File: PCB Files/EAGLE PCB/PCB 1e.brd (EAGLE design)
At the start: 45 x 75 mm, 31 parts

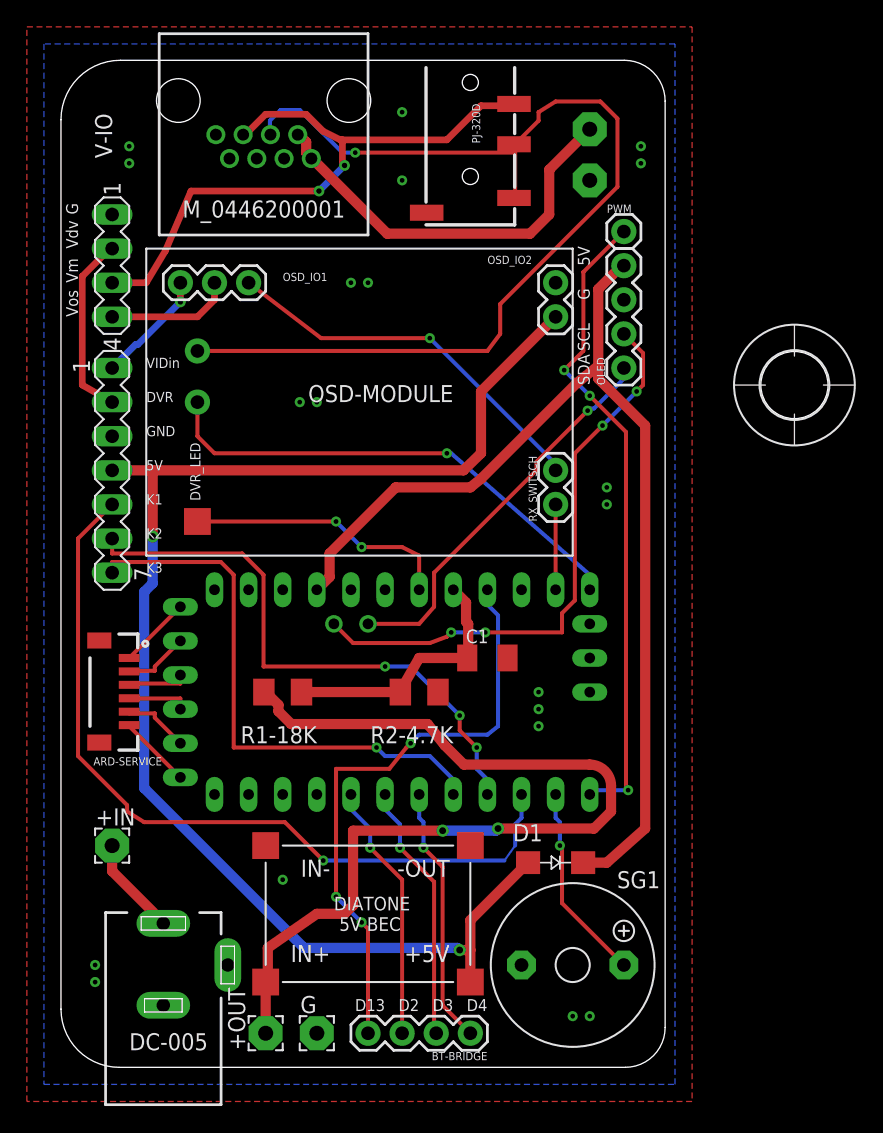
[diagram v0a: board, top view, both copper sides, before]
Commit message: new pcb1 revision 3 (5v on RJ45 and OSD PCB footprint added)
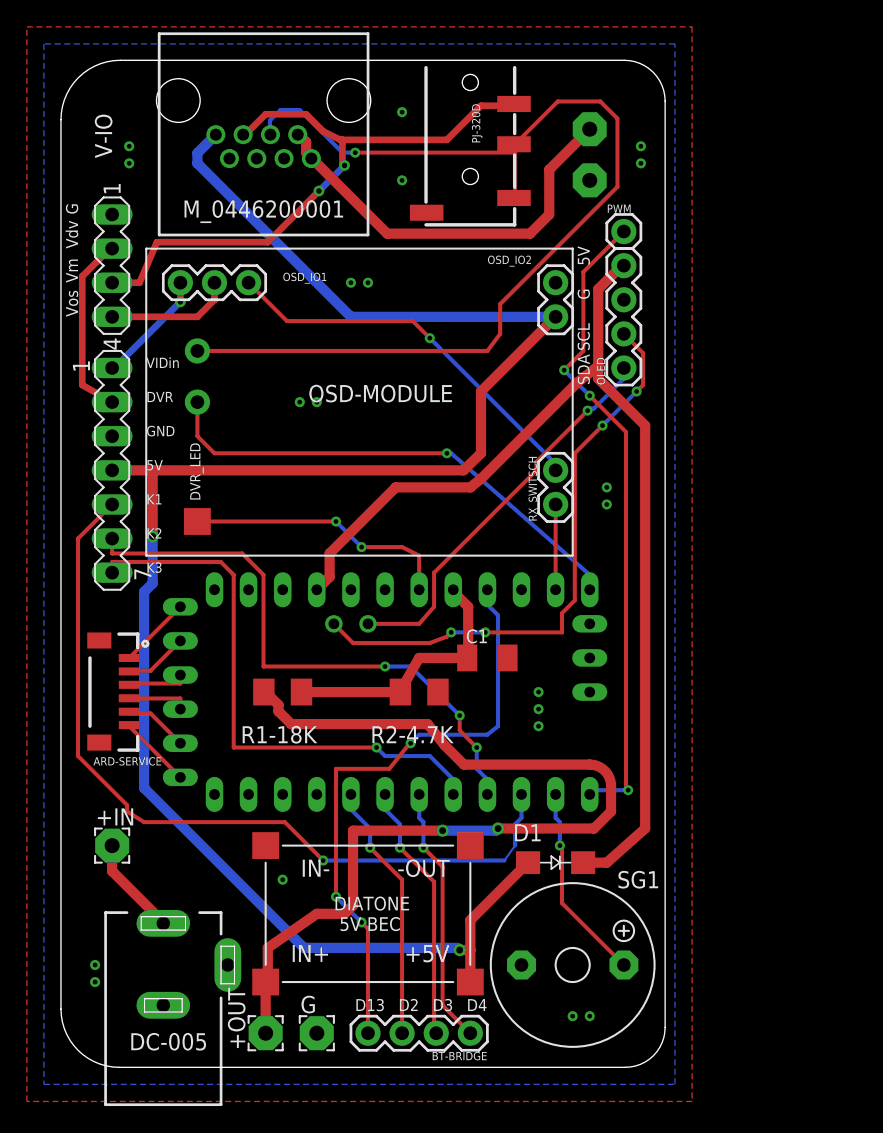
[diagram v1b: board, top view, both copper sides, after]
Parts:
- removed U$2: (no value), holes:5,0
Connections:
- net +5V: now also M_0446200001.1
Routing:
- net +5V: track 104.3 -> 138.4 mm
- net VMAIN: track 46.9 -> 46.2 mm

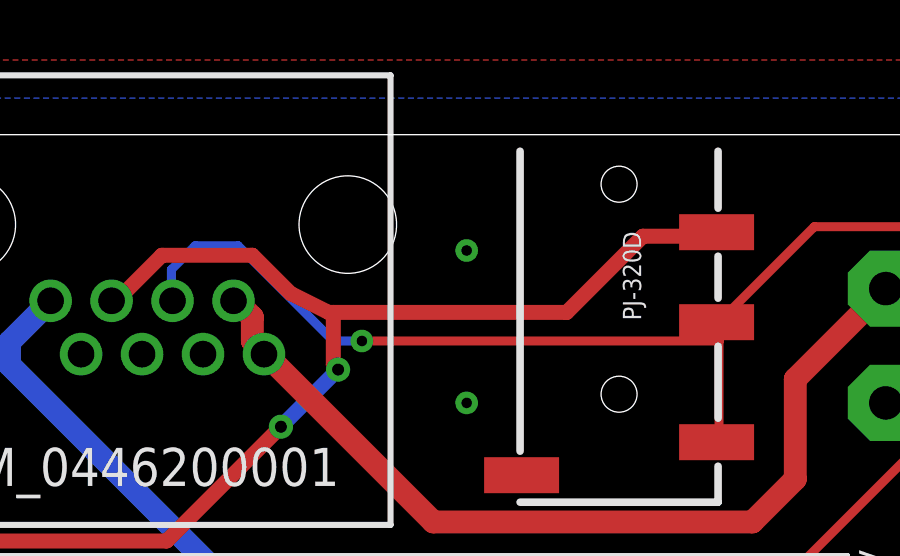
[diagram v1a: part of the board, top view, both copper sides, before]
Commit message: added 75ohm resistor to pcb
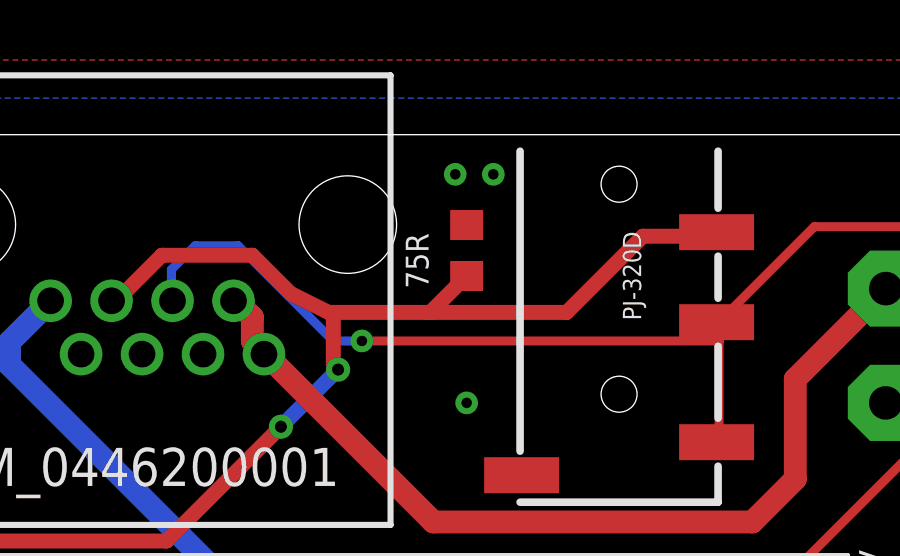
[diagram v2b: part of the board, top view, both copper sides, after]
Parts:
- added 75R: 75, resistor:R0603
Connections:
- net GND: now also 75R.2
- net VMAIN: now also 75R.1
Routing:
- net VMAIN: track 46.2 -> 47.9 mm
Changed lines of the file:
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@@
 <attribute name="VALUE" x="7.62" y="56.388" size="0.6096" layer="27" font="vector" ratio="20"/>
+</element>
+<element name="75R" library="resistor" library_urn="urn:adsk.eagle:library:348" package="R0603" package3d_urn="urn:adsk.eagle:package:23555/2" value="75" x="25.4" y="71.12" smashed="yes" rot="R90">
+<attribute name="NAME" x="24.13" y="69.85" size="0.762" layer="25" rot="R90"/>
+<attribute name="VALUE" x="27.94" y="69.85" size="1.27" layer="27" rot="R90"/>
 </element>
 </elements>
@@
 <via x="5.08" y="68.58" extent="1-16" drill="0.35"/>
 <via x="5.08" y="67.31" extent="1-16" drill="0.35"/>
-<via x="25.4" y="71.12" extent="1-16" drill="0.35"/>
+<via x="25.019" y="73.66" extent="1-16" drill="0.35"/>
 <via x="25.4" y="66.04" extent="1-16" drill="0.35"/>
 <via x="43.18" y="67.31" extent="1-16" drill="0.35"/>
@@
 <via x="40.64" y="43.18" extent="1-16" drill="0.35"/>
 <via x="40.64" y="41.91" extent="1-16" drill="0.35"/>
+<contactref element="75R" pad="2"/>
+<via x="26.289" y="73.66" extent="1-16" drill="0.35"/>
 </signal>
 <signal name="RAWVIDEO_MODULE" class="2">
@@
 <wire x1="28.73375" y1="69.05625" x2="31.27375" y2="71.59625" width="0.5" layer="1"/>
 <wire x1="20.79625" y1="69.05625" x2="20.955" y2="69.05625" width="0.5" layer="1"/>
-<wire x1="20.955" y1="69.05625" x2="28.73375" y2="69.05625" width="0.5" layer="1"/>
+<wire x1="20.955" y1="69.05625" x2="24.13" y2="69.05625" width="0.5" layer="1"/>
+<wire x1="24.18625" y1="69.05625" x2="28.73375" y2="69.05625" width="0.5" layer="1"/>
 <wire x1="19.52625" y1="69.69125" x2="20.79625" y2="69.05625" width="0.5" layer="1"/>
 <wire x1="18.25625" y1="70.96125" x2="19.52625" y2="69.69125" width="0.5" layer="1"/>
@@
 <wire x1="15.24" y1="70.96125" x2="13.81125" y2="69.5325" width="0.5" layer="1"/>
 <wire x1="13.81125" y1="69.5325" x2="13.6525" y2="69.5325" width="0.1524" layer="1"/>
+<contactref element="75R" pad="1"/>
+<wire x1="25.4" y1="70.27" x2="24.18625" y2="69.05625" width="0.5" layer="1"/>
+<wire x1="24.18625" y1="69.05625" x2="24.13" y2="69.05625" width="0.5" layer="1"/>
 </signal>
 <signal name="LED" class="1">
